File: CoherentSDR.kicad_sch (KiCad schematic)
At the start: 0 parts

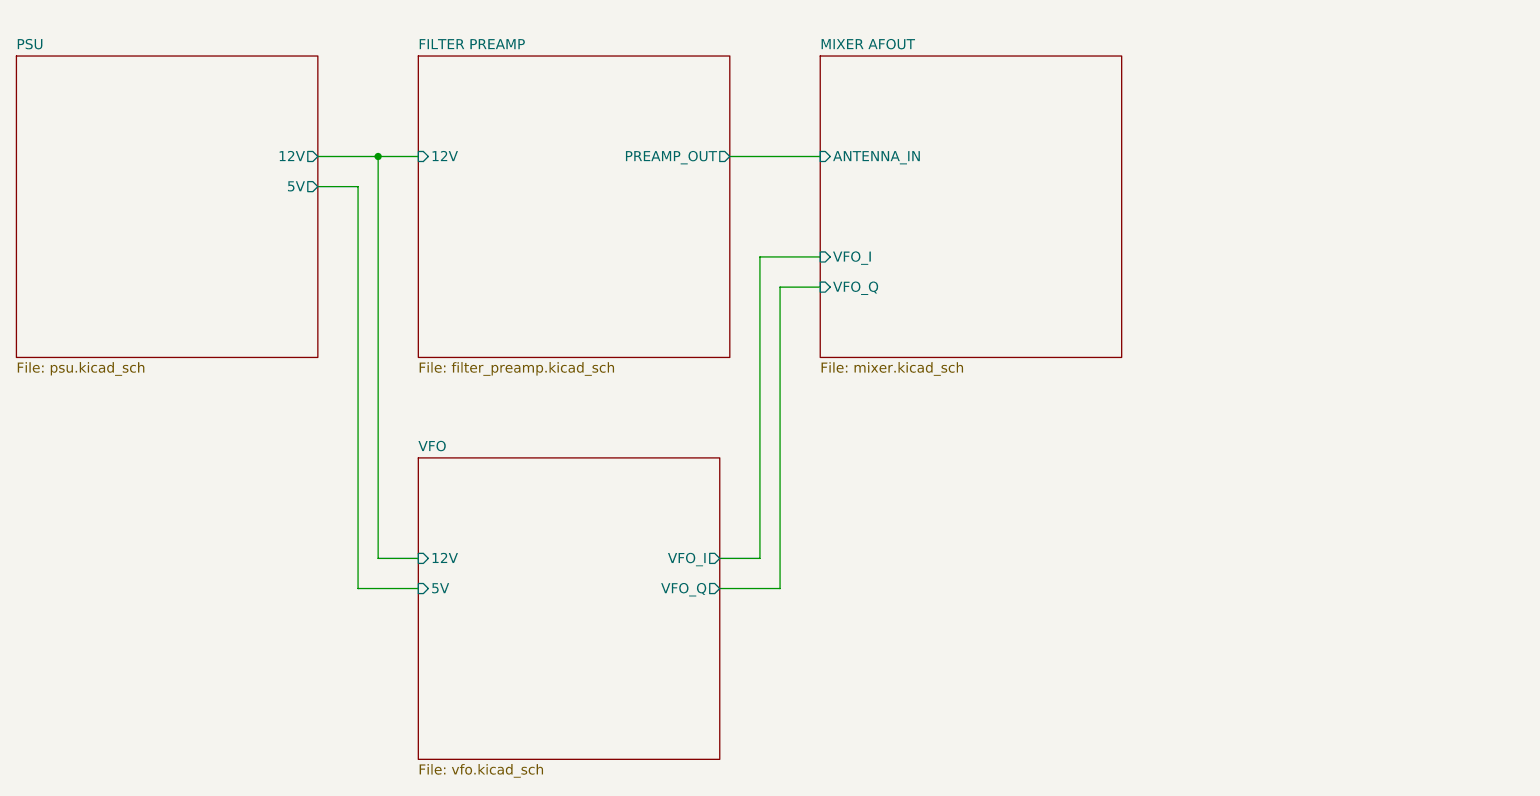
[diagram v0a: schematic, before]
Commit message: Rework RF amplifier design and add AF amplification
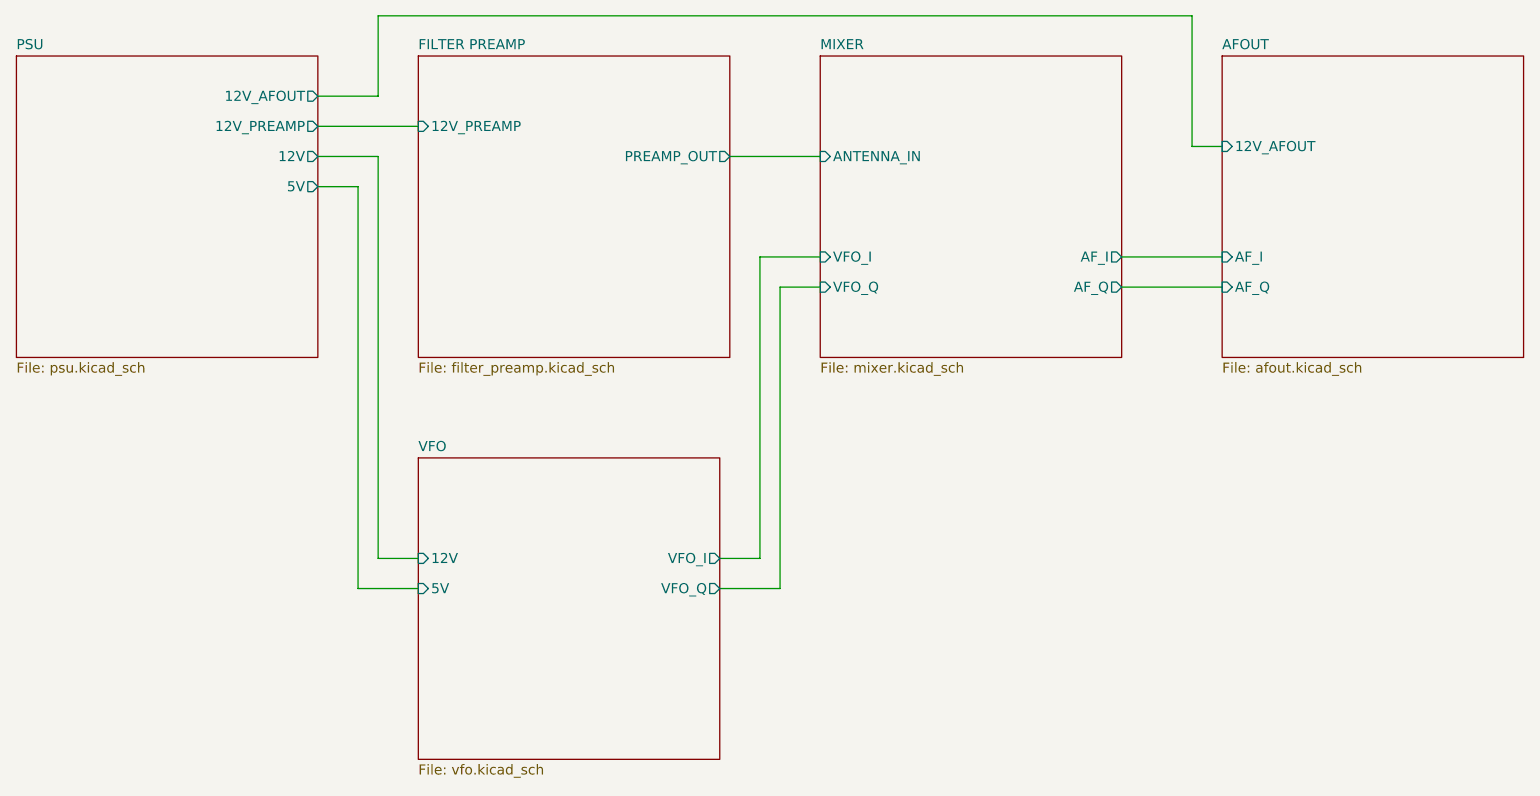
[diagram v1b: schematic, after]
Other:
- sheet MIXER AFOUT renamed MIXER
- added sheet AFOUT (afout.kicad_sch)
- sheet FILTER PREAMP ports: added 12V_PREAMP; removed 12V
- sheet MIXER ports: added AF_I, AF_Q; removed none
- sheet PSU ports: added 12V_AFOUT, 12V_PREAMP; removed none
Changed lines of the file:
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@@
 	(generator_version "9.0")
 	(paper "A4")
-	(junction
-		(at 96.52 63.5)
-		(diameter 0)
-		(color 0 0 0 0)
+	(wire
+		(pts
+			(xy 190.5 76.2) (xy 203.2 76.2)
+		)
+		(stroke
+			(width 0)
+			(type default)
+		)
 	)
 	(wire
@@
 	(wire
 		(pts
+			(xy 190.5 80.01) (xy 203.2 80.01)
+		)
+		(stroke
+			(width 0)
+			(type default)
+		)
+	)
+	(wire
+		(pts
 			(xy 88.9 63.5) (xy 96.52 63.5)
 		)
@@
 	(wire
 		(pts
+			(xy 96.52 45.72) (xy 96.52 55.88)
+		)
+		(stroke
+			(width 0)
+			(type default)
+		)
+	)
+	(wire
+		(pts
 			(xy 147.32 80.01) (xy 152.4 80.01)
 		)
@@
 	(wire
 		(pts
+			(xy 96.52 45.72) (xy 199.39 45.72)
+		)
+		(stroke
+			(width 0)
+			(type default)
+		)
+	)
+	(wire
+		(pts
+			(xy 88.9 55.88) (xy 96.52 55.88)
+		)
+		(stroke
+			(width 0)
+			(type default)
+		)
+	)
+	(wire
+		(pts
 			(xy 139.7 118.11) (xy 147.32 118.11)
 		)
@@
 	(wire
 		(pts
+			(xy 88.9 59.69) (xy 101.6 59.69)
+		)
+		(stroke
+			(width 0)
+			(type default)
+		)
+	)
+	(wire
+		(pts
 			(xy 93.98 67.31) (xy 93.98 118.11)
 		)
@@
 	(wire
 		(pts
-			(xy 96.52 63.5) (xy 101.6 63.5)
+			(xy 199.39 45.72) (xy 199.39 62.23)
+		)
+		(stroke
+			(width 0)
+			(type default)
+		)
+	)
+	(wire
+		(pts
+			(xy 199.39 62.23) (xy 203.2 62.23)
 		)
 		(stroke
@@
 	)
 	(sheet
+		(at 203.2 50.8)
+		(size 38.1 38.1)
+		(exclude_from_sim no)
+		(in_bom yes)
+		(on_board yes)
+		(dnp no)
+		(fields_autoplaced yes)
+		(stroke
+			(width 0.1524)
+			(type solid)
+		)
+		(fill
+			(color 0 0 0 0.0000)
+		)
+		(property "Sheetname" "AFOUT"
+			(at 203.2 50.0884 0)
+			(effects
+				(font
+					(size 1.27 1.27)
+				)
+				(justify left bottom)
+			)
+		)
+		(property "Sheetfile" "afout.kicad_sch"
+			(at 203.2 89.4846 0)
+			(effects
+				(font
+					(size 1.27 1.27)
+				)
+				(justify left top)
+			)
+		)
+		(pin "12V_AFOUT" input
+			(at 203.2 62.23 180)
+			(effects
+				(font
+					(size 1.27 1.27)
+				)
+				(justify left)
+			)
+		)
+		(pin "AF_I" input
+			(at 203.2 76.2 180)
+			(effects
+				(font
+					(size 1.27 1.27)
+				)
+				(justify left)
+			)
+		)
+		(pin "AF_Q" input
+			(at 203.2 80.01 180)
+			(effects
+				(font
+					(size 1.27 1.27)
+				)
+				(justify left)
+			)
+		)
+		(instances
+			(project "CoherentSDR"
+				(path "/156bbb46-a717-4de3-b783-cbb954a57d2b"
+					(page "6")
+				)
+			)
+		)
+	)
+	(sheet
 		(at 152.4 50.8)
 		(size 38.1 38.1)
@@
 			(color 0 0 0 0.0000)
 		)
-		(property "Sheetname" "MIXER AFOUT"
+		(property "Sheetname" "MIXER"
 			(at 152.4 50.0884 0)
 			(effects
@@
 				)
 				(justify left)
+			)
+		)
+		(pin "AF_I" output
+			(at 190.5 76.2 0)
+			(effects
+				(font
+					(size 1.27 1.27)
+				)
+				(justify right)
+			)
+		)
+		(pin "AF_Q" output
+			(at 190.5 80.01 0)
+			(effects
+				(font
+					(size 1.27 1.27)
+				)
+				(justify right)
 			)
 		)
@@
 			)
 		)
+		(pin "12V_AFOUT" output
+			(at 88.9 55.88 0)
+			(effects
+				(font
+					(size 1.27 1.27)
+				)
+				(justify right)
+			)
+		)
+		(pin "12V_PREAMP" output
+			(at 88.9 59.69 0)
+			(effects
+				(font
+					(size 1.27 1.27)
+				)
+				(justify right)
+			)
+		)
 		(instances
 			(project "CoherentSDR"
@@
 			)
 		)
-		(pin "12V" input
-			(at 101.6 63.5 180)
-			(effects
-				(font
+		(pin "12V_PREAMP" input
+			(at 101.6 59.69 180)
+			(effects
+				(font
